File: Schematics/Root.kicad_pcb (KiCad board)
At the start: 2 copper layers, 100 x 100 mm, 137 parts, among them CON1 USB-MICRO-B, CON2 BARREL_JACK, IC1 ATXMEGA256A3BU-A, J1 AVR_JTAG_Header, P1 CONN_02X08, SW1 SW_PUSH, SW2 SW_PUSH, SW3 SW_PUSH, SW4 SW_PUSH, U1 PCA9685, U10 PCA9685, U11 PCA9685, U12 PCA9685, U13 LT8612, U2 PCA9685, U3 PCA9685, U4 PCA9685, U5 PCA9685, U6 PCA9685, U7 PCA9685, U8 PCA9685, U9 PCA9685, X1 16MHz, X2 32.768KhZ

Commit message: Sorted silkscreen out. Added a select to change function of one of the switches to between a reset or a general purpose
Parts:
- added JP2: JUMPER, Resistors_SMD:R_0603, F.Cu at (111.6, 65.8)
- added JP3: JUMPER, Resistors_SMD:R_0603, F.Cu at (111.6, 67.3)
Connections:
- net Net-(IC1-Pad6) renamed /Microcontroller/SW1
- net Net-(IC1-Pad8) renamed /Microcontroller/SW3
- net Net-(IC1-Pad9) renamed /Microcontroller/SW4
- CON1 pad 1: (no net) -> Net-(CON1-Pad1)
- IC1 pad 1: (no net) -> Net-(IC1-Pad1)
- IC1 pad 2: (no net) -> Net-(IC1-Pad2)
- IC1 pad 3: (no net) -> Net-(IC1-Pad3)
- IC1 pad 36: (no net) -> Net-(IC1-Pad36)
- IC1 pad 37: (no net) -> Net-(IC1-Pad37)
- IC1 pad 38: (no net) -> Net-(IC1-Pad38)
- IC1 pad 39: (no net) -> Net-(IC1-Pad39)
- IC1 pad 4: (no net) -> Net-(IC1-Pad4)
- IC1 pad 40: (no net) -> Net-(IC1-Pad40)
- IC1 pad 46: (no net) -> Net-(IC1-Pad46)
- IC1 pad 47: (no net) -> Net-(IC1-Pad47)
- IC1 pad 5: (no net) -> Net-(IC1-Pad5)
- IC1 pad 54: (no net) -> Net-(IC1-Pad54)
- IC1 pad 55: (no net) -> Net-(IC1-Pad55)
- IC1 pad 56: (no net) -> Net-(IC1-Pad56)
- IC1 pad 7: Net-(IC1-Pad7) -> /Microcontroller/SW2
- J1 pad 7: (no net) -> Net-(J1-Pad7)
- J1 pad 8: (no net) -> Net-(J1-Pad8)
- SW2 pad 1: Net-(IC1-Pad7) -> Net-(JP2-Pad2)
- U1 pad 22: (no net) -> Net-(U1-Pad22)
- U10 pad 22: (no net) -> Net-(U10-Pad22)
- U11 pad 22: (no net) -> Net-(U11-Pad22)
- U12 pad 22: (no net) -> Net-(U12-Pad22)
- U2 pad 22: (no net) -> Net-(U2-Pad22)
- U3 pad 22: (no net) -> Net-(U3-Pad22)
- U4 pad 22: (no net) -> Net-(U4-Pad22)
- U5 pad 22: (no net) -> Net-(U5-Pad22)
- U6 pad 22: (no net) -> Net-(U6-Pad22)
- U7 pad 22: (no net) -> Net-(U7-Pad22)
- U8 pad 22: (no net) -> Net-(U8-Pad22)
- U9 pad 22: (no net) -> Net-(U9-Pad22)
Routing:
- net Net-(IC1-Pad7): track 22.3 -> 0.00 mm, vias 2 -> 0
- net /Microcontroller/SW2: track 0.00 -> 11.3 mm, vias 0 -> 2
- net Net-(JP2-Pad2): track 0.00 -> 10.9 mm
- net /Microcontroller/~RESET: track 18.3 -> 24.8 mm
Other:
- board text added: "seblovett RGB Clock V1.0 www.github.com/seblovett/RGB_Clock"

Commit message: Added clock face to silkscreen
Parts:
- added G***: LOGO, Numbers:clock_face, B.Cu at (139.7, 83.0)

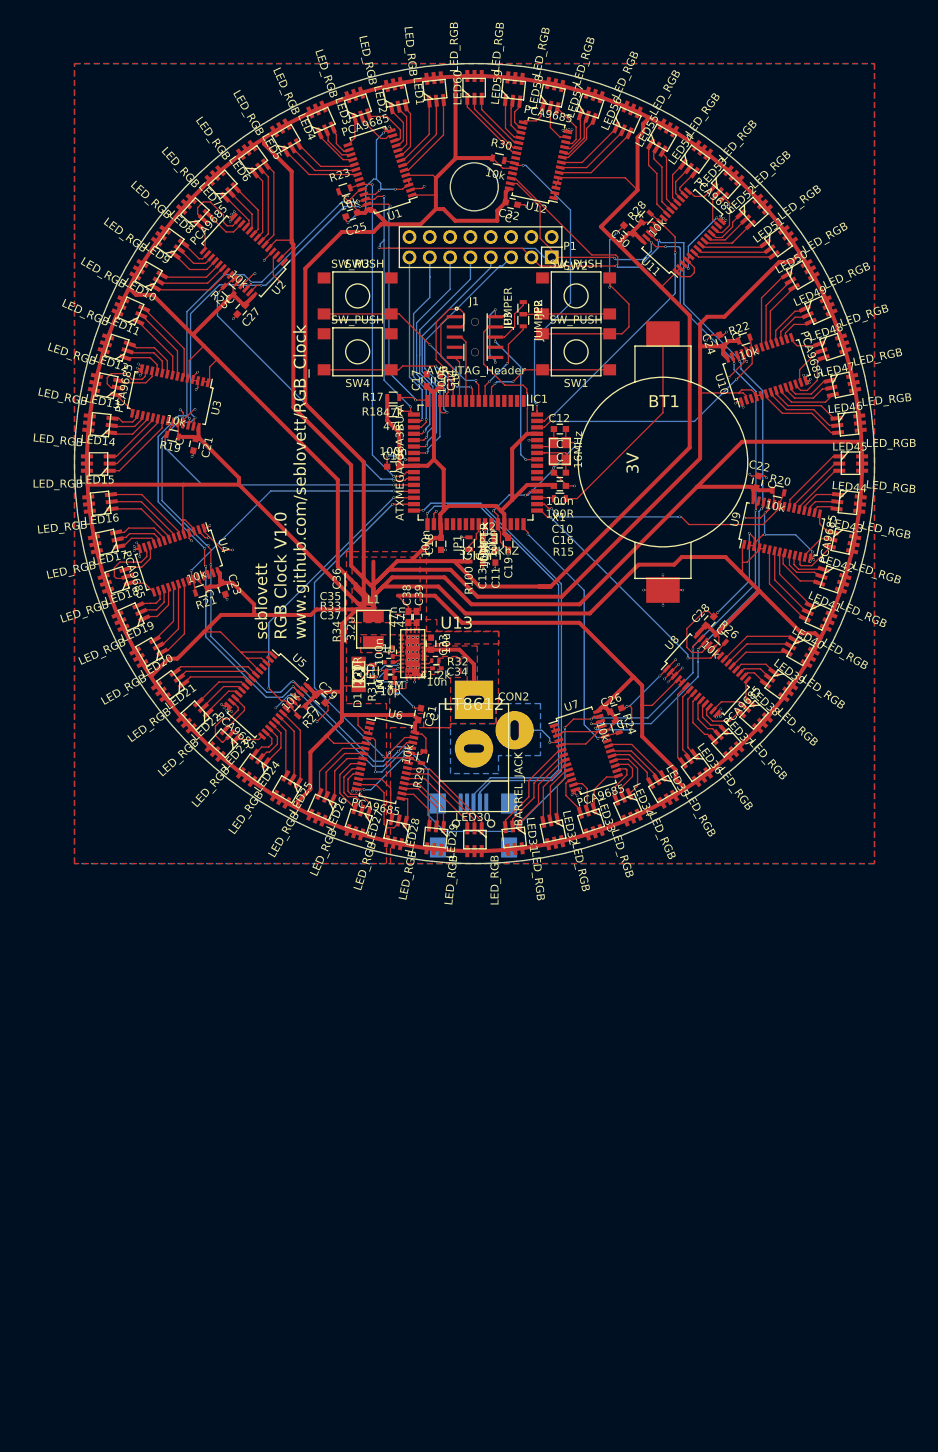
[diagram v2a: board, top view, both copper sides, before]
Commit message: Completed layout of 10cm board. Fixes #8
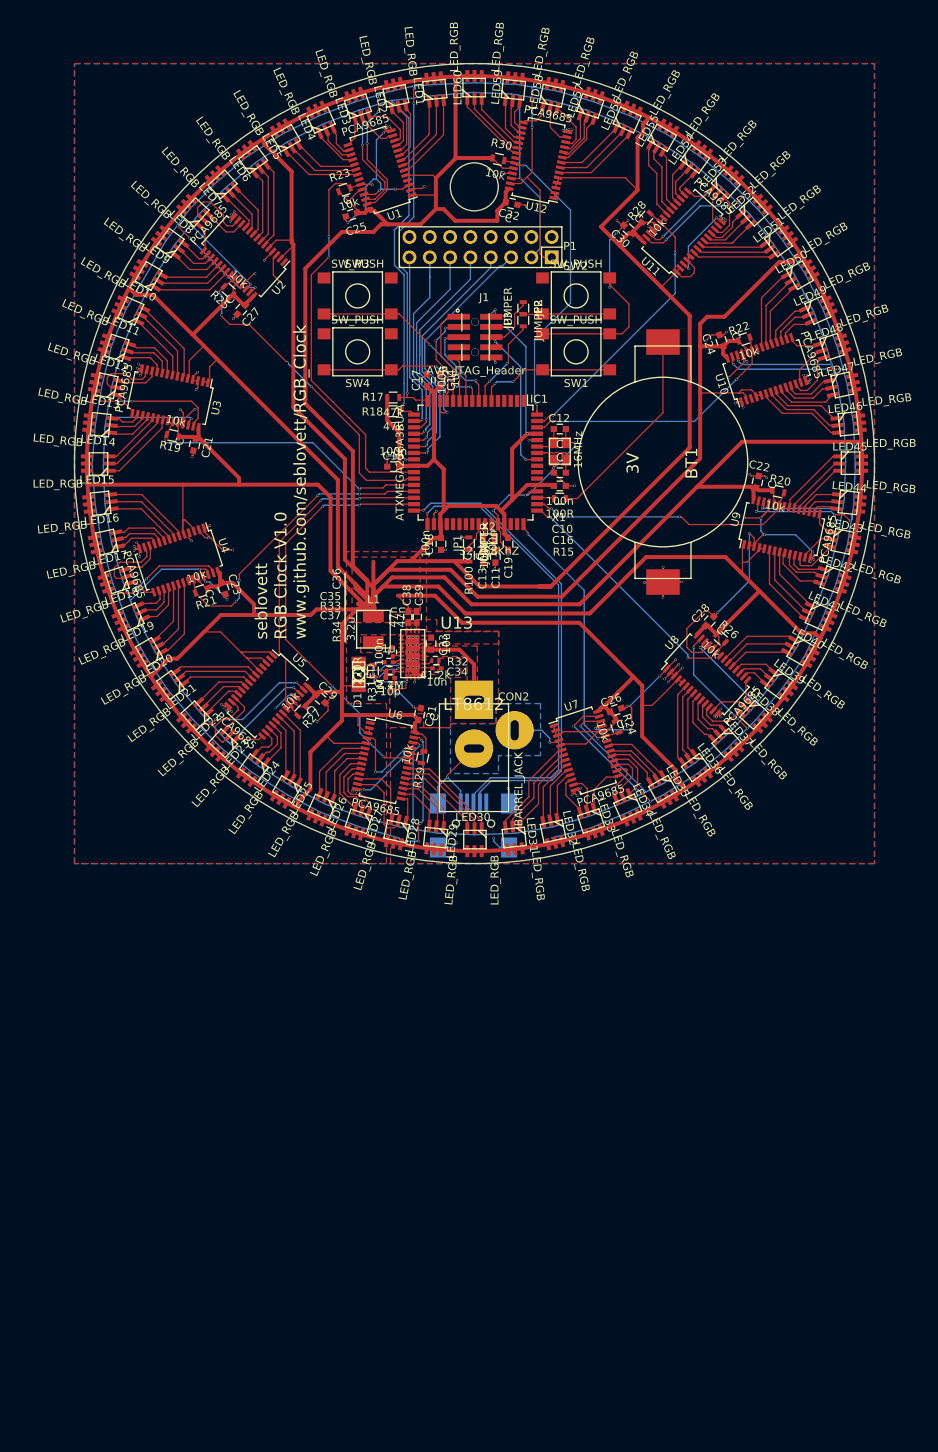
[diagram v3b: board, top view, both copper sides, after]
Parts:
- removed G***: LOGO, Numbers:clock_face
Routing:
- net /Display/SCL: track 291.6 -> 492.5 mm, vias 16 -> 14
- net /Display/SDA: track 322.0 -> 518.5 mm, vias 17 -> 39
- net GND: track 360.7 -> 391.0 mm, vias 141 -> 150
- net /Display/Display Sub block 6/~OE: track 46.9 -> 54.9 mm, vias 2 -> 6
- net /Display/Display Sub block 1/~OE: track 43.5 -> 51.2 mm, vias 2 -> 3
- net /Microcontroller/TDO: track 17.6 -> 12.1 mm, vias 0 -> 2
- net VPP: track 1368.5 -> 1373.7 mm, vias 2 -> 4
- net /Display/Display Sub block 5/~OE: track 38.0 -> 42.5 mm, vias 2 -> 4
- net /Display/Display Sub block 4/~OE: track 35.1 -> 37.6 mm, vias 2 -> 4
- net /Display/Display Sub block 2/~OE: track 38.8 -> 41.3 mm, vias 2 -> 7
- net /Microcontroller/TMS: track 9.03 -> 10.7 mm, vias 0 -> 2
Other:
- board text added: "Absolute maximum current all LEDs can draw is 6A. Averages to 0.55A per track. At this rating, need at least 0.12mm track for 10C rise. We have 0.5 so easily safe"
- board text added: "Vin track - 3A 10C rise 4A 20C rise. 6A - 50C rise. Getting too hot for this, but cannot afford a thicker track."

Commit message: Started Redesign.
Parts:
- removed C21, C22, C23, C24, C25, C26, C27, C28, C29, C30, C31, C32: C, Capacitors_SMD:C_0603
- removed LED1, LED10, LED11, LED12, LED13, LED14, LED15, LED16, LED17, LED18, LED19, LED2, LED20, LED21, LED22, LED23, LED24, LED25, LED26, LED27, LED28, LED29, LED3, LED30, LED31, LED32, LED33, LED34, LED35, LED36, LED37, LED38, LED39, LED4, LED40, LED41, LED42, LED43, LED44, LED45, LED46, LED47, LED48, LED49, LED5, LED50, LED51, LED52, LED53, LED54, LED55, LED56, LED57, LED58, LED59, LED6, LED60, LED7, LED8, LED9: LED_RGB, rgb:rgbled1
- removed R19, R20, R21, R22, R23, R24, R25, R26, R27, R28, R29, R30: 10k, Resistors_SMD:R_0603
- removed SW3, SW4: SW_PUSH, rgb:SW
- removed U1, U10, U11, U12, U2, U3, U4, U5, U6, U7, U8, U9: PCA9685, Housings_SSOP:TSSOP-28_4.4x9.7mm_Pitch0.65mm
- added P10: CONN_01X06, JST-SH:JST-BM-06B-SRSS-TB, F.Cu at (52.2, 160.4)
- added P100: CONN_02X08, Socket_Strips:Socket_Strip_Straight_2x08, F.Cu at (70.2, 137.8)
- added P11: CONN_01X06, JST-SH:JST-BM-06B-SRSS-TB, F.Cu at (55.4, 152.5)
- added P12: CONN_01X06, JST-SH:JST-BM-06B-SRSS-TB, F.Cu at (72.3, 152.5)
- added P2: CONN_01X06, JST-SH:JST-BM-06B-SRSS-TB, F.Cu at (97.4, 160.8)
- added P3: CONN_01X06, JST-SH:JST-BM-06B-SRSS-TB, F.Cu at (97.4, 170.3)
- added P4: CONN_01X06, JST-SH:JST-BM-06B-SRSS-TB, F.Cu at (97.4, 179.7)
- added P5: CONN_01X06, JST-SH:JST-BM-06B-SRSS-TB, F.Cu at (79.5, 197.5)
- added P6: CONN_01X06, JST-SH:JST-BM-06B-SRSS-TB, F.Cu at (69.6, 197.5)
- added P7: CONN_01X06, JST-SH:JST-BM-06B-SRSS-TB, F.Cu at (52.2, 189.4)
- added P8: CONN_01X06, JST-SH:JST-BM-06B-SRSS-TB, F.Cu at (52.2, 179.7)
- added P9: CONN_01X06, JST-SH:JST-BM-06B-SRSS-TB, F.Cu at (52.2, 170.2)
- BT1, C33, C34, C35, C36, C37, C38, C39, JP2, JP3, L1, R32, R33, R34, U13: moved to B.Cu
- C10, C12: value C -> 33pF
- C11, C13: value C -> 22pF
- P1: value CONN_02X08 -> CONN_01X06; footprint Socket_Strips:Socket_Strip_Straight_2x08 -> JST-SH:JST-BM-06B-SRSS-TB
- moved C17 113.6 mm to (77.8, 186.3), turned to 270 degrees
- moved BT1 110.1 mm to (64.4, 174.1)
- moved JP2 109.8 mm to (79.0, 170.6), turned to 180 degrees
- moved C14 109.1 mm to (64.1, 177.4), turned to 180 degrees
- moved JP3 108.8 mm to (77.5, 170.6), turned to 0 degrees
- moved SW1 105.3 mm to (64.9, 162.1), turned to 270 degrees
- moved SW2 104.4 mm to (81.6, 162.1), turned to 270 degrees
- moved C19 99.4 mm to (69.8, 186.3)
- moved JP1 97.7 mm to (73.2, 187.6), turned to 270 degrees
- moved C12 97.1 mm to (84.5, 172.7)
- moved X1 97.0 mm to (84.6, 175.3)
- moved J1 96.8 mm to (74.3, 161.0), turned to 90 degrees
- moved R17 96.8 mm to (64.1, 168.5)
- moved R18 96.7 mm to (64.1, 170.2)
- moved C11 96.4 mm to (76.3, 187.8)
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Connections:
- net /Display/SCL renamed /Microcontroller/SCL
- CON1 pad 1: Net-(CON1-Pad1) -> (no net)
- IC1 pad 1: Net-(IC1-Pad1) -> (no net)
- IC1 pad 16: /Display/SDA -> /Microcontroller/SDA
- IC1 pad 2: Net-(IC1-Pad2) -> (no net)
- IC1 pad 26: /Display/Display Sub block 1/~OE -> (no net)
- IC1 pad 27: /Display/Display Sub block 2/~OE -> (no net)
- IC1 pad 28: /Display/Display Sub block 3/~OE -> (no net)
- IC1 pad 29: /Display/Display Sub block 4/~OE -> (no net)
- IC1 pad 3: Net-(IC1-Pad3) -> (no net)
- IC1 pad 30: /Display/Display Sub block 5/~OE -> (no net)
- IC1 pad 31: /Display/Display Sub block 6/~OE -> (no net)
- IC1 pad 36: Net-(IC1-Pad36) -> (no net)
- IC1 pad 37: Net-(IC1-Pad37) -> (no net)
- IC1 pad 38: Net-(IC1-Pad38) -> (no net)
- IC1 pad 39: Net-(IC1-Pad39) -> (no net)
- IC1 pad 4: Net-(IC1-Pad4) -> (no net)
- IC1 pad 40: Net-(IC1-Pad40) -> (no net)
- IC1 pad 46: Net-(IC1-Pad46) -> (no net)
- IC1 pad 47: Net-(IC1-Pad47) -> (no net)
- IC1 pad 48: /Display/Display Sub block 7/~OE -> (no net)
- IC1 pad 49: /Display/Display Sub block 8/~OE -> (no net)
- IC1 pad 5: Net-(IC1-Pad5) -> (no net)
- IC1 pad 50: /Display/Display Sub block 9/~OE -> (no net)
- IC1 pad 54: Net-(IC1-Pad54) -> (no net)
- IC1 pad 55: Net-(IC1-Pad55) -> (no net)
- IC1 pad 56: Net-(IC1-Pad56) -> (no net)
- IC1 pad 62: /Display/Display Sub block 10/~OE -> (no net)
- IC1 pad 63: /Display/Display Sub block 11/~OE -> (no net)
- IC1 pad 64: /Display/Display Sub block 12/~OE -> (no net)
- J1 pad 7: Net-(J1-Pad7) -> (no net)
- J1 pad 8: Net-(J1-Pad8) -> (no net)
- P1 pad 1: /Display/SDA -> VPP
- P1 pad 2: GND -> /Microcontroller/SDA
- P1 pad 5: /Microcontroller/SCK -> (no net)
- R17 pad 2: /Display/SDA -> /Microcontroller/SDA
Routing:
- net VPP: track 1373.7 -> 0.00 mm, vias 4 -> 0
- net /Display/SDA: track 518.5 -> 0.00 mm, vias 39 -> 0
- net /Microcontroller/SCL: track 492.5 -> 0.00 mm, vias 14 -> 0
- net GND: track 391.0 -> 0.00 mm, vias 150 -> 0
- net /Microcontroller/USB_D-: track 59.0 -> 0.00 mm, vias 1 -> 0
- net /Microcontroller/USB_D+: track 58.2 -> 0.00 mm, vias 1 -> 0
- net /Display/Display Sub block 6/~OE: track 54.9 -> 0.00 mm, vias 6 -> 0
- net /Display/Display Sub block 1/~OE: track 51.2 -> 0.00 mm, vias 3 -> 0
- net /Display/Display Sub block 5/~OE: track 42.5 -> 0.00 mm, vias 4 -> 0
- net /Display/Display Sub block 2/~OE: track 41.3 -> 0.00 mm, vias 7 -> 0
- net /Display/Display Sub block 12/~OE: track 38.3 -> 0.00 mm, vias 2 -> 0
- net /Display/Display Sub block 4/~OE: track 37.6 -> 0.00 mm, vias 4 -> 0
- net /Display/Display Sub block 3/~OE: track 36.6 -> 0.00 mm, vias 2 -> 0
- net /Display/Display Sub block 11/~OE: track 35.2 -> 0.00 mm, vias 2 -> 0
- net /Display/Display Sub block 9/~OE: track 34.2 -> 0.00 mm, vias 2 -> 0
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- removed copper zone on F.Cu, net /Power Supply/SW
- removed copper zone on F.Cu, net /Power Supply/Vin
- removed copper zone on B.Cu, net GND
- removed copper zone on F.Cu, net GND
- removed copper zone on F.Cu, net VPP
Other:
- board size 100 x 100 mm -> 50 x 50 mm
- net class Default: clearance 0.15 -> 0.254; trace_width 0.15 -> 0.254; via_dia 0.3 -> 0.889; via_drill 0.25 -> 0.635
- net class Power removed
- rule trace_clearance: 0.15 -> 0.254
- rule trace_min: 0.15 -> 0.254
- rule via_min_drill: 0.25 -> 0.508
- rule via_min_size: 0.3 -> 0.889
- board text removed: "Absolute maximum current all LEDs can draw is 6A. Averages to 0.55A per track. At this rating, need at least 0.12mm track for 10C rise. We have 0.5 so easily safe"
- board text removed: "Vin track - 3A 10C rise 4A 20C rise. 6A - 50C rise. Getting too hot for this, but cannot afford a thicker track."
- board text removed: "seblovett RGB Clock V1.0 www.github.com/seblovett/RGB_Clock"

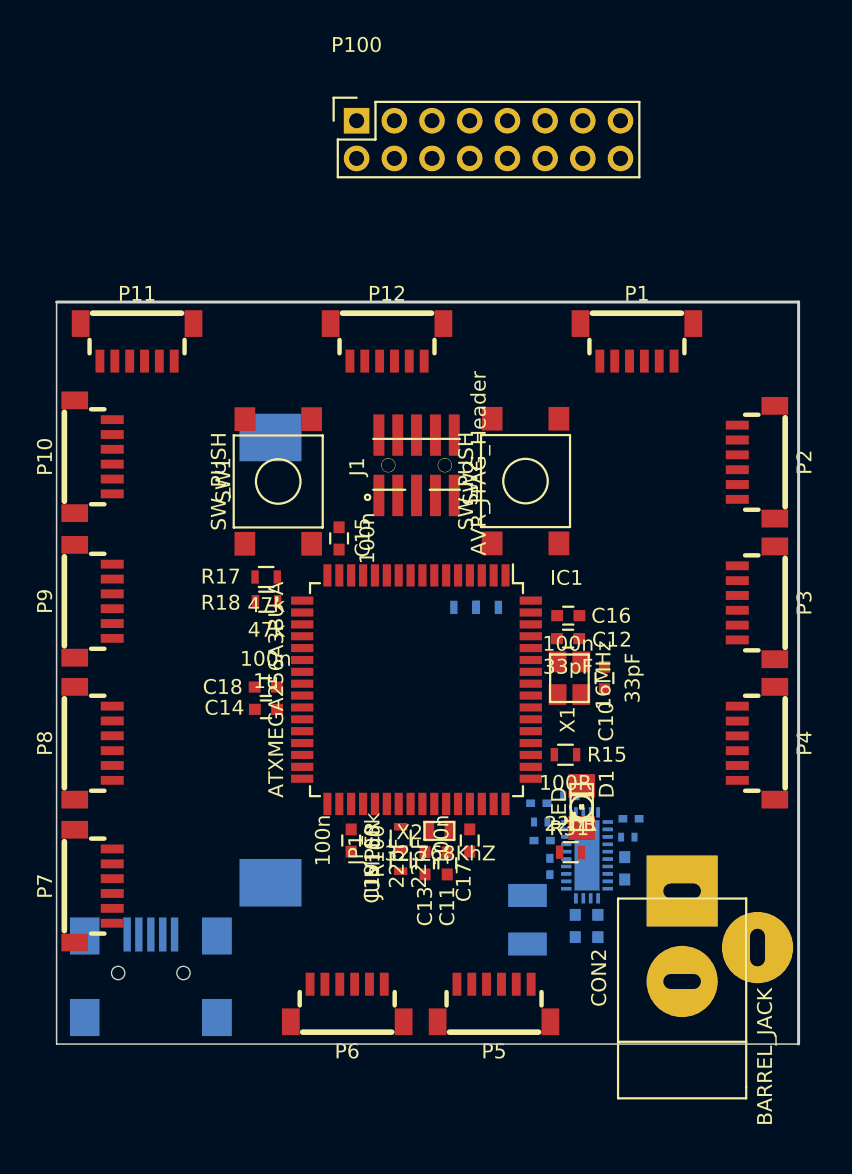
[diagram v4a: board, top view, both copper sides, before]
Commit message: Done some more layout.
Need to sort pin swaps for the OE lines and complete routing
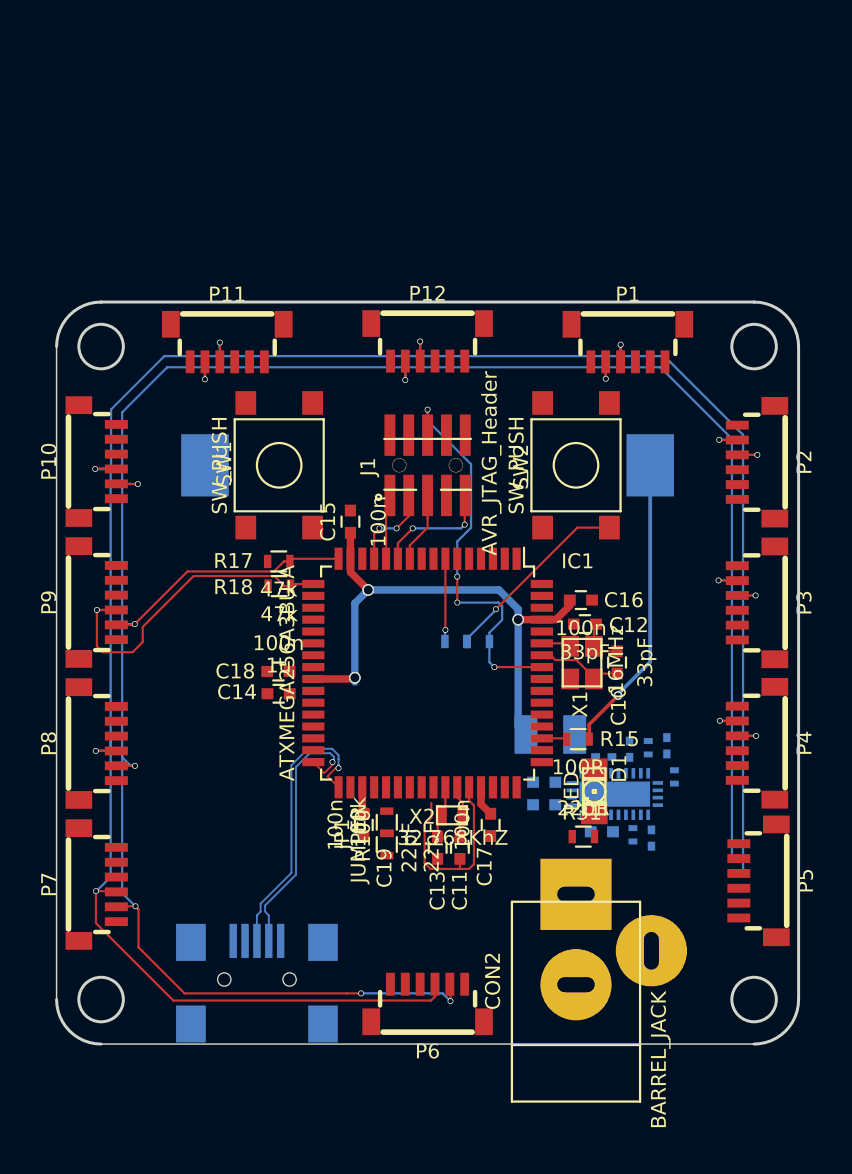
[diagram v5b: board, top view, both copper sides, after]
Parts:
- removed P100: CONN_02X08, Socket_Strips:Socket_Strip_Straight_2x08
- moved P5 19.9 mm to (97.5, 189.0), turned to 270 degrees
- moved BT1 16.9 mm to (75.0, 161.0), turned to 180 degrees
- moved L1 12.6 mm to (83.3, 179.1), turned to 180 degrees
- moved C39 9.91 mm to (82.9, 182.4), turned to 0 degrees
- moved C37 9.46 mm to (91.1, 179.9), turned to 270 degrees
- moved C38 8.93 mm to (82.9, 183.9), turned to 0 degrees
- moved R33 8.80 mm to (89.9, 180.0), turned to 270 degrees
- moved C35 8.52 mm to (88.6, 180.1), turned to 90 degrees
- moved C36 8.22 mm to (86.9, 180.7), turned to 0 degrees
- moved CON1 7.16 mm to (63.5, 196.5)
- moved R34 7.15 mm to (91.6, 182.0), turned to 270 degrees
- moved CON2 7.15 mm to (85.0, 196.0)
- moved P11 6.08 mm to (61.5, 152.5)
- moved P6 5.42 mm to (75.0, 197.5)
- moved U13 4.54 mm to (87.6, 183.2), turned to 90 degrees
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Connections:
- IC1 pad 18: /Microcontroller/RX -> (no net)
- IC1 pad 19: /Microcontroller/TX -> (no net)
- IC1 pad 20: /Microcontroller/~CS -> (no net)
- IC1 pad 21: /Microcontroller/MOSI -> (no net)
- IC1 pad 22: /Microcontroller/MISO -> (no net)
- IC1 pad 23: /Microcontroller/SCK -> (no net)
- IC1 pad 26: (no net) -> /~OE1
- IC1 pad 27: (no net) -> /~OE2
- IC1 pad 28: (no net) -> /~OE3
- IC1 pad 29: (no net) -> /~OE4
- IC1 pad 30: (no net) -> /~OE5
- IC1 pad 31: (no net) -> /~OE6
- IC1 pad 48: (no net) -> /~OE7
- IC1 pad 49: (no net) -> /~OE8
- IC1 pad 50: (no net) -> /~OE9
- IC1 pad 62: (no net) -> /~OE10
- IC1 pad 63: (no net) -> /~OE11
- IC1 pad 64: (no net) -> /~OE12
- IC1 pad 8: /Microcontroller/SW3 -> (no net)
- IC1 pad 9: /Microcontroller/SW4 -> (no net)
- P1 pad 5: (no net) -> /~OE1
- P10 pad 5: (no net) -> /~OE10
- P11 pad 5: (no net) -> /~OE11
- P12 pad 5: (no net) -> /~OE12
- P2 pad 5: (no net) -> /~OE2
- P3 pad 5: (no net) -> /~OE3
- P4 pad 5: (no net) -> /~OE4
- P5 pad 5: (no net) -> /~OE5
- P6 pad 5: (no net) -> /~OE6
- P7 pad 5: (no net) -> /~OE7
- P8 pad 5: (no net) -> /~OE8
- P9 pad 5: (no net) -> /~OE9
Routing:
- net /Microcontroller/SCL: track 0.00 -> 180.9 mm, vias 0 -> 10
- net /Microcontroller/SDA: track 0.00 -> 169.1 mm, vias 0 -> 12
- net VPP: track 0.00 -> 41.4 mm, vias 0 -> 3
- net /Microcontroller/~RESET: track 0.00 -> 27.2 mm, vias 0 -> 4
- net Net-(BT1-Pad1): track 0.00 -> 20.2 mm, vias 0 -> 1
- net /Microcontroller/USB_D+: track 0.00 -> 19.5 mm, vias 0 -> 1
- net /Microcontroller/USB_D-: track 0.00 -> 18.1 mm, vias 0 -> 1
- net GND: track 0.00 -> 17.9 mm
- net Net-(JP2-Pad2): track 0.00 -> 12.9 mm, vias 0 -> 1
- net /Microcontroller/TDI: track 0.00 -> 8.05 mm, vias 0 -> 2
- net /Microcontroller/TDO: track 0.00 -> 6.00 mm, vias 0 -> 2
- net Net-(C10-Pad1): track 0.00 -> 5.94 mm
- net /Microcontroller/SW2: track 0.00 -> 5.69 mm, vias 0 -> 1
- net /Microcontroller/TMS: track 0.00 -> 4.77 mm
- net /Microcontroller/TCK: track 0.00 -> 4.38 mm
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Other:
- outline, holes or cut-outs redrawn
- net class Default: clearance 0.254 -> 0.15; trace_width 0.254 -> 0.15; via_dia 0.889 -> 0.4; via_drill 0.635 -> 0.3
- net class Power added: clearance 0.15, trace_width 0.5, via_dia 0.8, via_drill 0.6
- rule trace_clearance: 0.254 -> 0.15
- rule trace_min: 0.254 -> 0.15
- rule via_min_drill: 0.508 -> 0.3
- rule via_min_size: 0.889 -> 0.3
